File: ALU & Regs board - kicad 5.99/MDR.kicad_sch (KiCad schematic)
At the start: 31 parts, among them U12 MC74ACT04DG, U51 MC74ACT157DG, U52 MC74ACT157DG, U53 MC74ACT273DWG, U54 MC74ACT273DWG, U55 MC74ACT244DWG, U56 MC74ACT244DWG, U57 MC74ACT244DWG, U58 MC74ACT244DWG, U59 MC74ACT244DWG, U60 MC74ACT244DWG, U61 MC74ACT245DWG, U62 MC74ACT153DG, U63 MC74ACT153DG, U64 MC74ACT153DG, U65 MC74ACT153DG

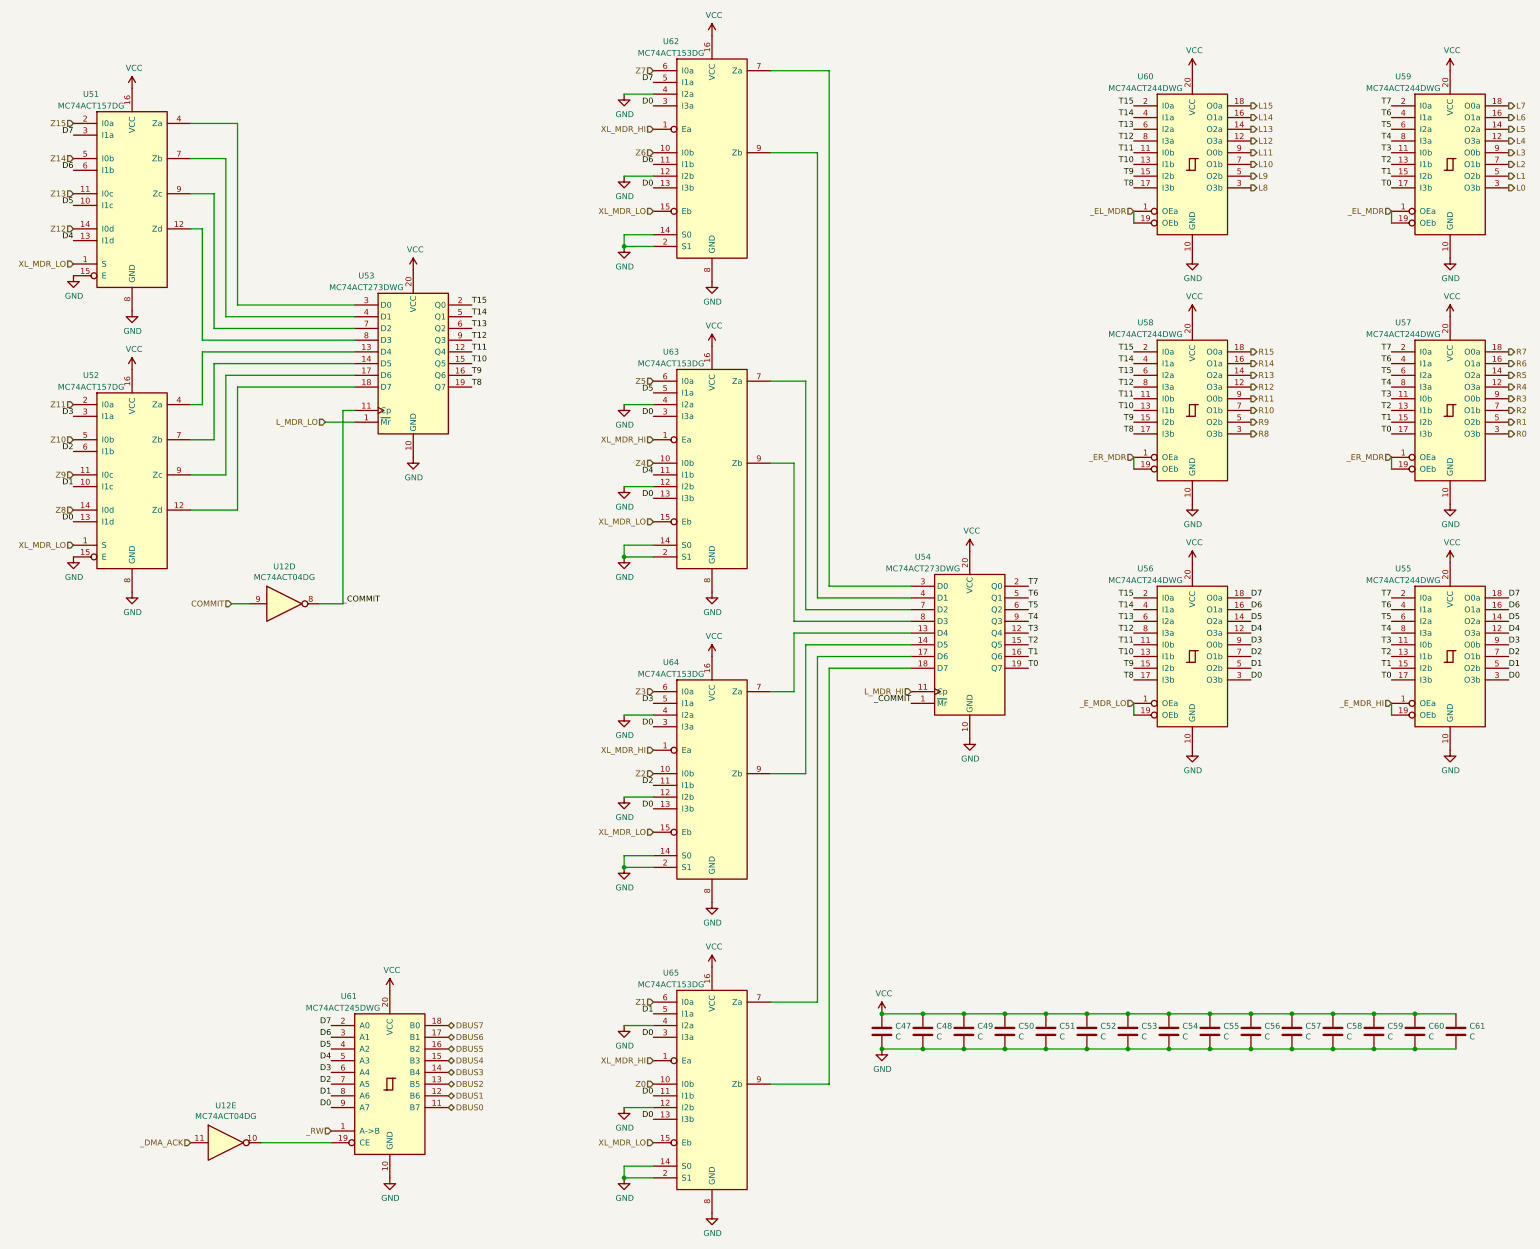
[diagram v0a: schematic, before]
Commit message: added a buffer on the _RESET line, which is rather loaded
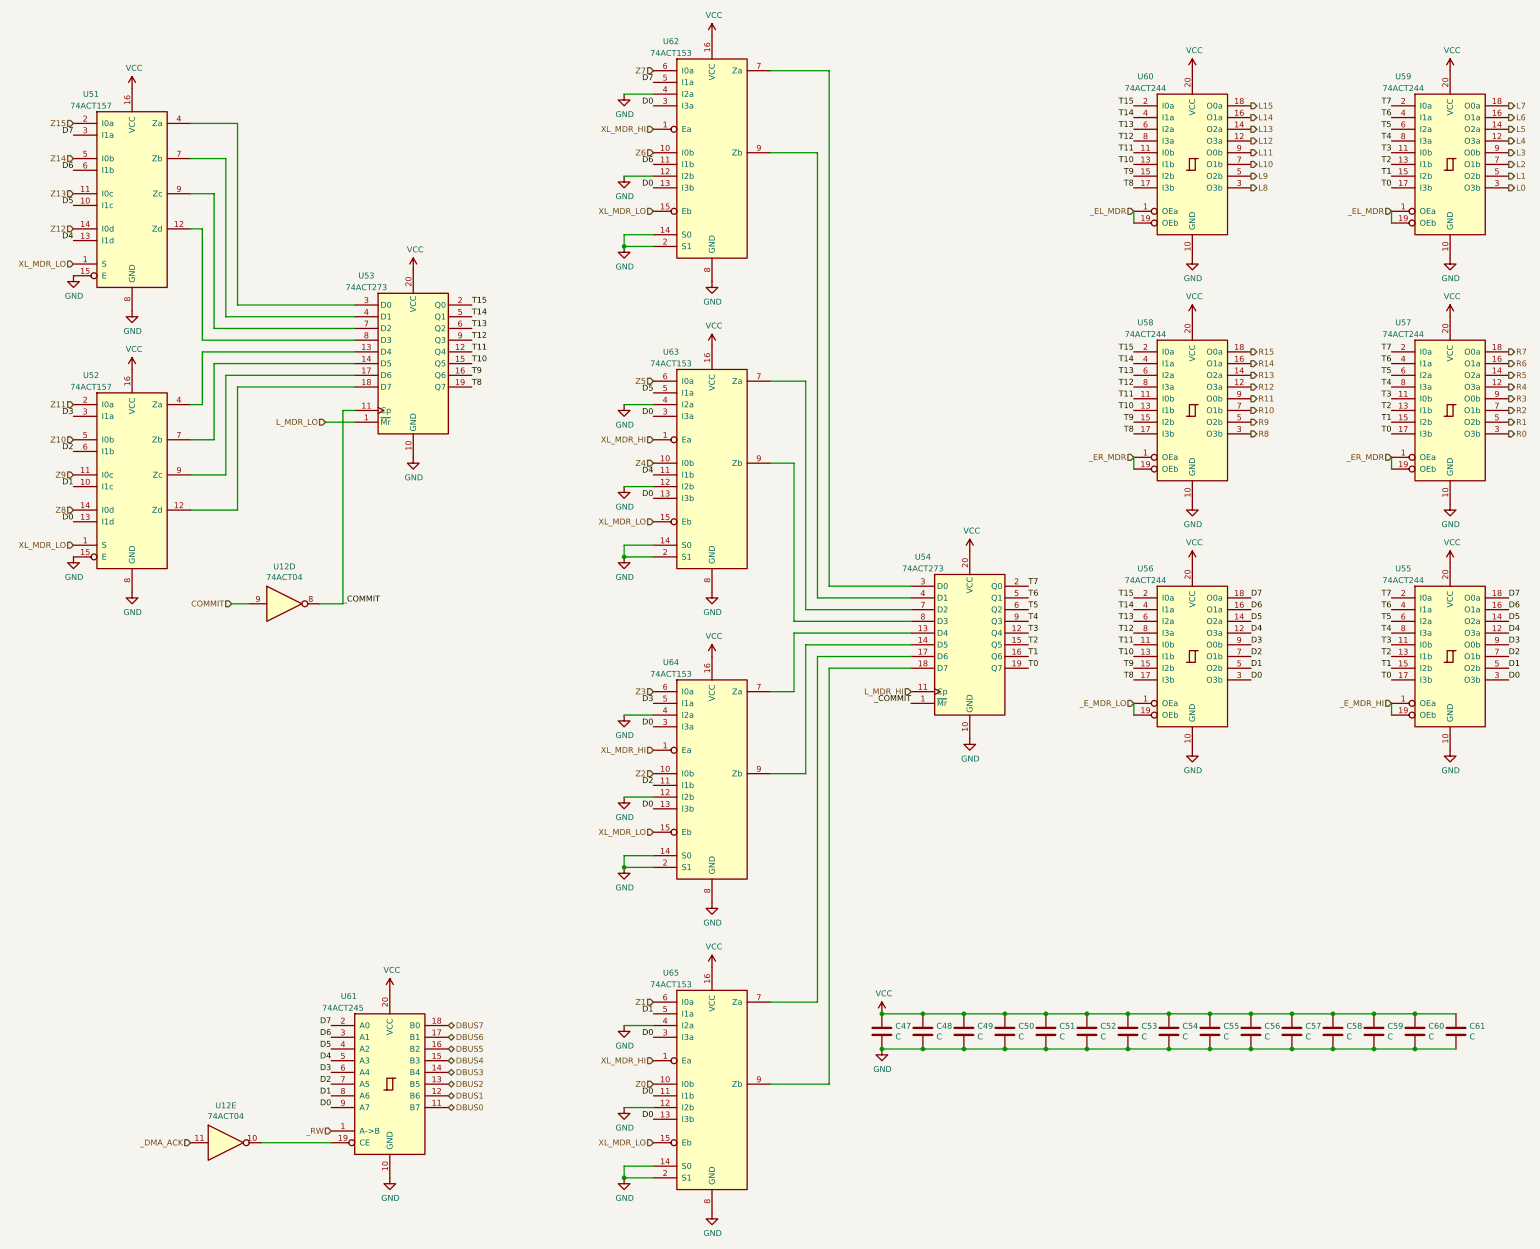
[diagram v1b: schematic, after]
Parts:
- U12: value MC74ACT04DG -> 74ACT04
- U51, U52: value MC74ACT157DG -> 74ACT157
- U53, U54: value MC74ACT273DWG -> 74ACT273
- U55, U56, U57, U58, U59, U60: value MC74ACT244DWG -> 74ACT244
- U61: value MC74ACT245DWG -> 74ACT245
- U62, U63, U64, U65: value MC74ACT153DG -> 74ACT153
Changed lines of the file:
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@@
     (in_bom yes) (on_board yes)
     (property "Reference" "U12" (id 0) (at 63.5 252.2982 0))
-    (property "Value" "MC74ACT04DG" (id 1) (at 63.5 254.6096 0))
+    (property "Value" "74ACT04" (id 1) (at 63.5 254.6096 0))
     (property "Footprint" "Package_SO:SOIC-14_3.9x8.7mm_P1.27mm" (id 2) (at 63.5 260.35 0)
       (effects (font (size 1.27 1.27)) hide)
@@
     (in_bom yes) (on_board yes)
     (property "Reference" "U12" (id 0) (at 76.2 135.4582 0))
-    (property "Value" "MC74ACT04DG" (id 1) (at 76.2 137.7696 0))
+    (property "Value" "74ACT04" (id 1) (at 76.2 137.77 0))
     (property "Footprint" "Package_SO:SOIC-14_3.9x8.7mm_P1.27mm" (id 2) (at 76.2 143.51 0)
       (effects (font (size 1.27 1.27)) hide)
@@
     (in_bom yes) (on_board yes)
     (property "Reference" "U61" (id 0) (at 90.17 228.6 0))
-    (property "Value" "MC74ACT245DWG" (id 1) (at 88.9 231.14 0))
+    (property "Value" "74ACT245" (id 1) (at 88.9 231.14 0))
     (property "Footprint" "Package_SO:SOIC-20W_7.5x12.8mm_P1.27mm" (id 2) (at 99.06 247.65 0)
       (effects (font (size 1.27 1.27)) hide)
@@
     (in_bom yes) (on_board yes)
     (property "Reference" "U53" (id 0) (at 93.98 72.39 0))
-    (property "Value" "MC74ACT273DWG" (id 1) (at 93.98 74.93 0))
+    (property "Value" "74ACT273" (id 1) (at 93.98 74.93 0))
     (property "Footprint" "Package_SO:SOIC-20W_7.5x12.8mm_P1.27mm" (id 2) (at 104.14 91.44 0)
       (effects (font (size 1.27 1.27)) hide)
@@
     (in_bom yes) (on_board yes)
     (property "Reference" "U54" (id 0) (at 214.63 133.35 0))
-    (property "Value" "MC74ACT273DWG" (id 1) (at 214.63 135.89 0))
+    (property "Value" "74ACT273" (id 1) (at 214.63 135.89 0))
     (property "Footprint" "Package_SO:SOIC-20W_7.5x12.8mm_P1.27mm" (id 2) (at 224.79 152.4 0)
       (effects (font (size 1.27 1.27)) hide)
@@
     (in_bom yes) (on_board yes)
     (property "Reference" "U60" (id 0) (at 262.89 29.21 0))
-    (property "Value" "MC74ACT244DWG " (id 1) (at 262.89 31.75 0))
+    (property "Value" "74ACT244" (id 1) (at 262.89 31.75 0))
     (property "Footprint" "Package_SO:SOIC-20W_7.5x12.8mm_P1.27mm" (id 2) (at 273.05 48.26 0)
       (effects (font (size 1.27 1.27)) hide)
@@
     (in_bom yes) (on_board yes)
     (property "Reference" "U58" (id 0) (at 262.89 82.55 0))
-    (property "Value" "MC74ACT244DWG " (id 1) (at 262.89 85.09 0))
+    (property "Value" "74ACT244" (id 1) (at 262.89 85.09 0))
     (property "Footprint" "Package_SO:SOIC-20W_7.5x12.8mm_P1.27mm" (id 2) (at 273.05 101.6 0)
       (effects (font (size 1.27 1.27)) hide)
@@
     (in_bom yes) (on_board yes)
     (property "Reference" "U56" (id 0) (at 262.89 135.89 0))
-    (property "Value" "MC74ACT244DWG " (id 1) (at 262.89 138.43 0))
+    (property "Value" "74ACT244" (id 1) (at 262.89 138.43 0))
     (property "Footprint" "Package_SO:SOIC-20W_7.5x12.8mm_P1.27mm" (id 2) (at 273.05 154.94 0)
       (effects (font (size 1.27 1.27)) hide)
@@
     (in_bom yes) (on_board yes)
     (property "Reference" "U59" (id 0) (at 318.77 29.21 0))
-    (property "Value" "MC74ACT244DWG " (id 1) (at 318.77 31.75 0))
+    (property "Value" "74ACT244" (id 1) (at 318.77 31.75 0))
     (property "Footprint" "Package_SO:SOIC-20W_7.5x12.8mm_P1.27mm" (id 2) (at 328.93 48.26 0)
       (effects (font (size 1.27 1.27)) hide)
@@
     (in_bom yes) (on_board yes)
     (property "Reference" "U57" (id 0) (at 318.77 82.55 0))
-    (property "Value" "MC74ACT244DWG " (id 1) (at 318.77 85.09 0))
+    (property "Value" "74ACT244" (id 1) (at 318.77 85.09 0))
     (property "Footprint" "Package_SO:SOIC-20W_7.5x12.8mm_P1.27mm" (id 2) (at 328.93 101.6 0)
       (effects (font (size 1.27 1.27)) hide)
@@
     (in_bom yes) (on_board yes)
     (property "Reference" "U55" (id 0) (at 318.77 135.89 0))
-    (property "Value" "MC74ACT244DWG " (id 1) (at 318.77 138.43 0))
+    (property "Value" "74ACT244" (id 1) (at 318.77 138.43 0))
     (property "Footprint" "Package_SO:SOIC-20W_7.5x12.8mm_P1.27mm" (id 2) (at 328.93 154.94 0)
       (effects (font (size 1.27 1.27)) hide)
@@
     (in_bom yes) (on_board yes)
     (property "Reference" "U51" (id 0) (at 34.29 33.02 0))
-    (property "Value" "MC74ACT157DG" (id 1) (at 34.29 35.56 0))
+    (property "Value" "74ACT157" (id 1) (at 34.29 35.56 0))
     (property "Footprint" "Package_SO:SOIC-16_3.9x9.9mm_P1.27mm" (id 2) (at 43.18 54.61 0)
       (effects (font (size 1.27 1.27)) hide)
@@
     (in_bom yes) (on_board yes)
     (property "Reference" "U52" (id 0) (at 34.29 93.98 0))
-    (property "Value" "MC74ACT157DG" (id 1) (at 34.29 96.52 0))
+    (property "Value" "74ACT157" (id 1) (at 34.29 96.52 0))
     (property "Footprint" "Package_SO:SOIC-16_3.9x9.9mm_P1.27mm" (id 2) (at 43.18 115.57 0)
       (effects (font (size 1.27 1.27)) hide)
@@
     (in_bom yes) (on_board yes)
     (property "Reference" "U62" (id 0) (at 160.02 21.59 0))
-    (property "Value" "MC74ACT153DG" (id 1) (at 160.02 24.13 0))
+    (property "Value" "74ACT153" (id 1) (at 160.02 24.13 0))
     (property "Footprint" "Package_SO:SOIC-16_3.9x9.9mm_P1.27mm" (id 2) (at 168.91 45.72 0)
       (effects (font (size 1.27 1.27)) hide)
@@
     (in_bom yes) (on_board yes)
     (property "Reference" "U63" (id 0) (at 160.02 88.9 0))
-    (property "Value" "MC74ACT153DG" (id 1) (at 160.02 91.44 0))
+    (property "Value" "74ACT153" (id 1) (at 160.02 91.44 0))
     (property "Footprint" "Package_SO:SOIC-16_3.9x9.9mm_P1.27mm" (id 2) (at 168.91 113.03 0)
       (effects (font (size 1.27 1.27)) hide)
@@
     (in_bom yes) (on_board yes)
     (property "Reference" "U64" (id 0) (at 160.02 156.21 0))
-    (property "Value" "MC74ACT153DG" (id 1) (at 160.02 158.75 0))
+    (property "Value" "74ACT153" (id 1) (at 160.02 158.75 0))
     (property "Footprint" "Package_SO:SOIC-16_3.9x9.9mm_P1.27mm" (id 2) (at 168.91 180.34 0)
       (effects (font (size 1.27 1.27)) hide)
@@
     (in_bom yes) (on_board yes)
     (property "Reference" "U65" (id 0) (at 160.02 223.52 0))
-    (property "Value" "MC74ACT153DG" (id 1) (at 160.02 226.06 0))
+    (property "Value" "74ACT153" (id 1) (at 160.02 226.06 0))
     (property "Footprint" "Package_SO:SOIC-16_3.9x9.9mm_P1.27mm" (id 2) (at 168.91 247.65 0)
       (effects (font (size 1.27 1.27)) hide)
